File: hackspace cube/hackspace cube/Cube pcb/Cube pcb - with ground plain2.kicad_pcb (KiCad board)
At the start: 2 copper layers, 100 x 64.5 mm, 61 parts, among them J1 Conn_01x09 ( conector 1), J2 Conn_01x09 ( conector 2), J3 Conn_01x02 ( exstra ground co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, J4 Conn_01x14 ( Spare Ports ), Q1 BSS138, Q10 BSS138, Q11 BSS138, Q12 BSS138, Q13 BSS138, Q14 BSS138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

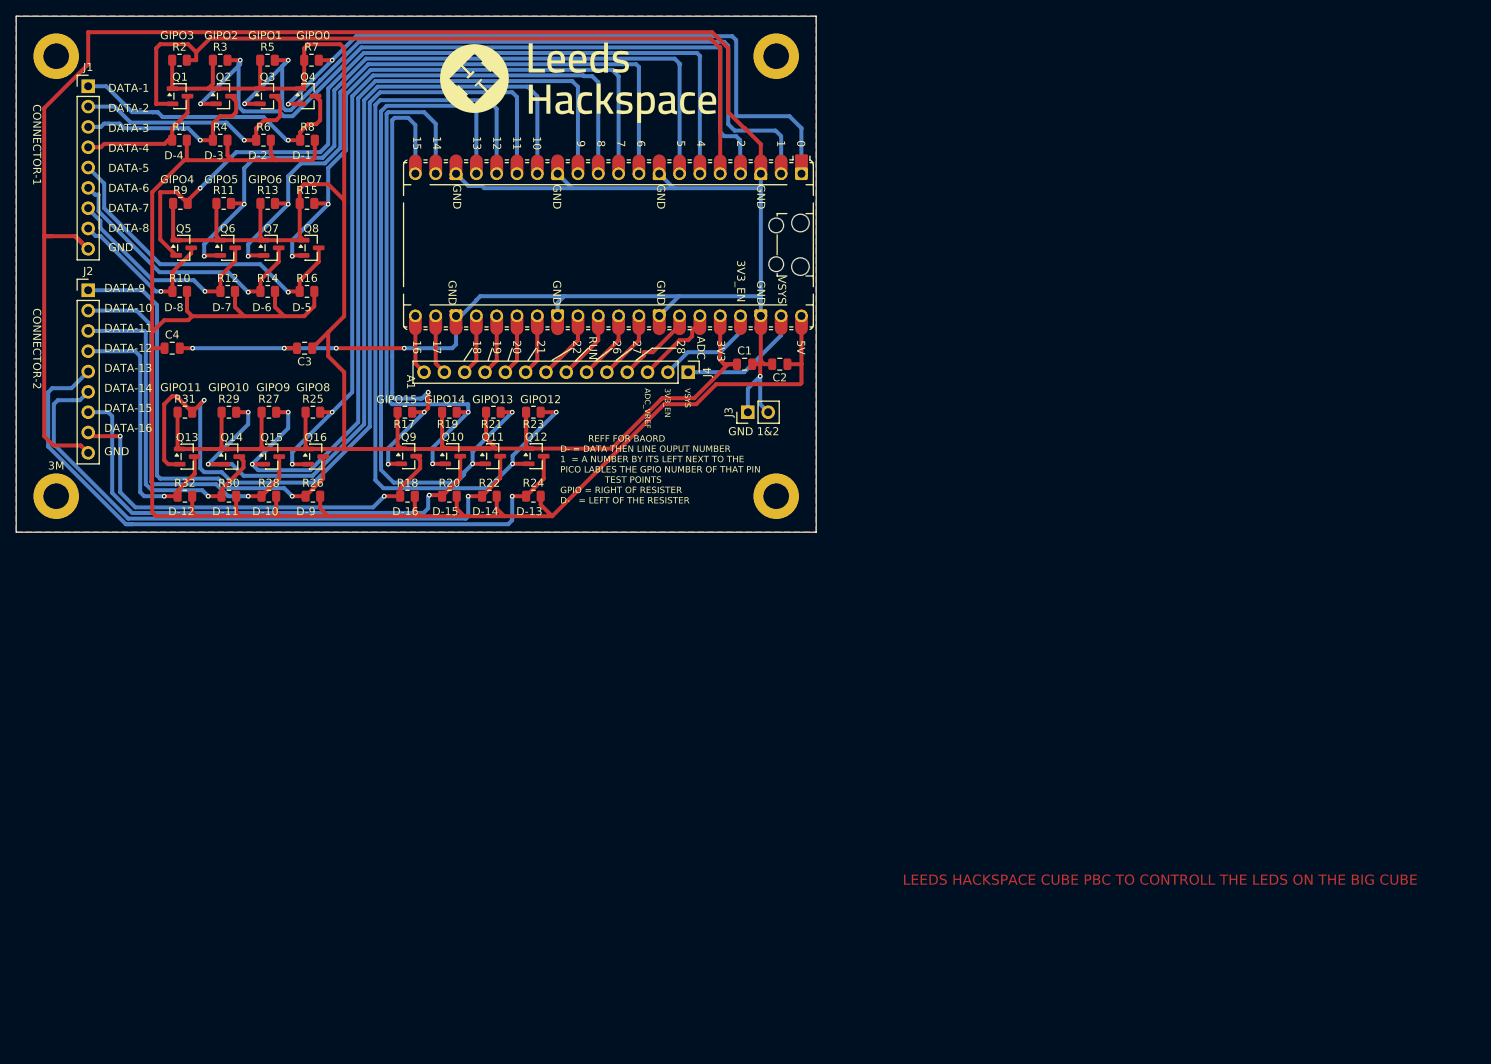
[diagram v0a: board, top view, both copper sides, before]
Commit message: rev 1.4
added new smooth caps and updated pcb
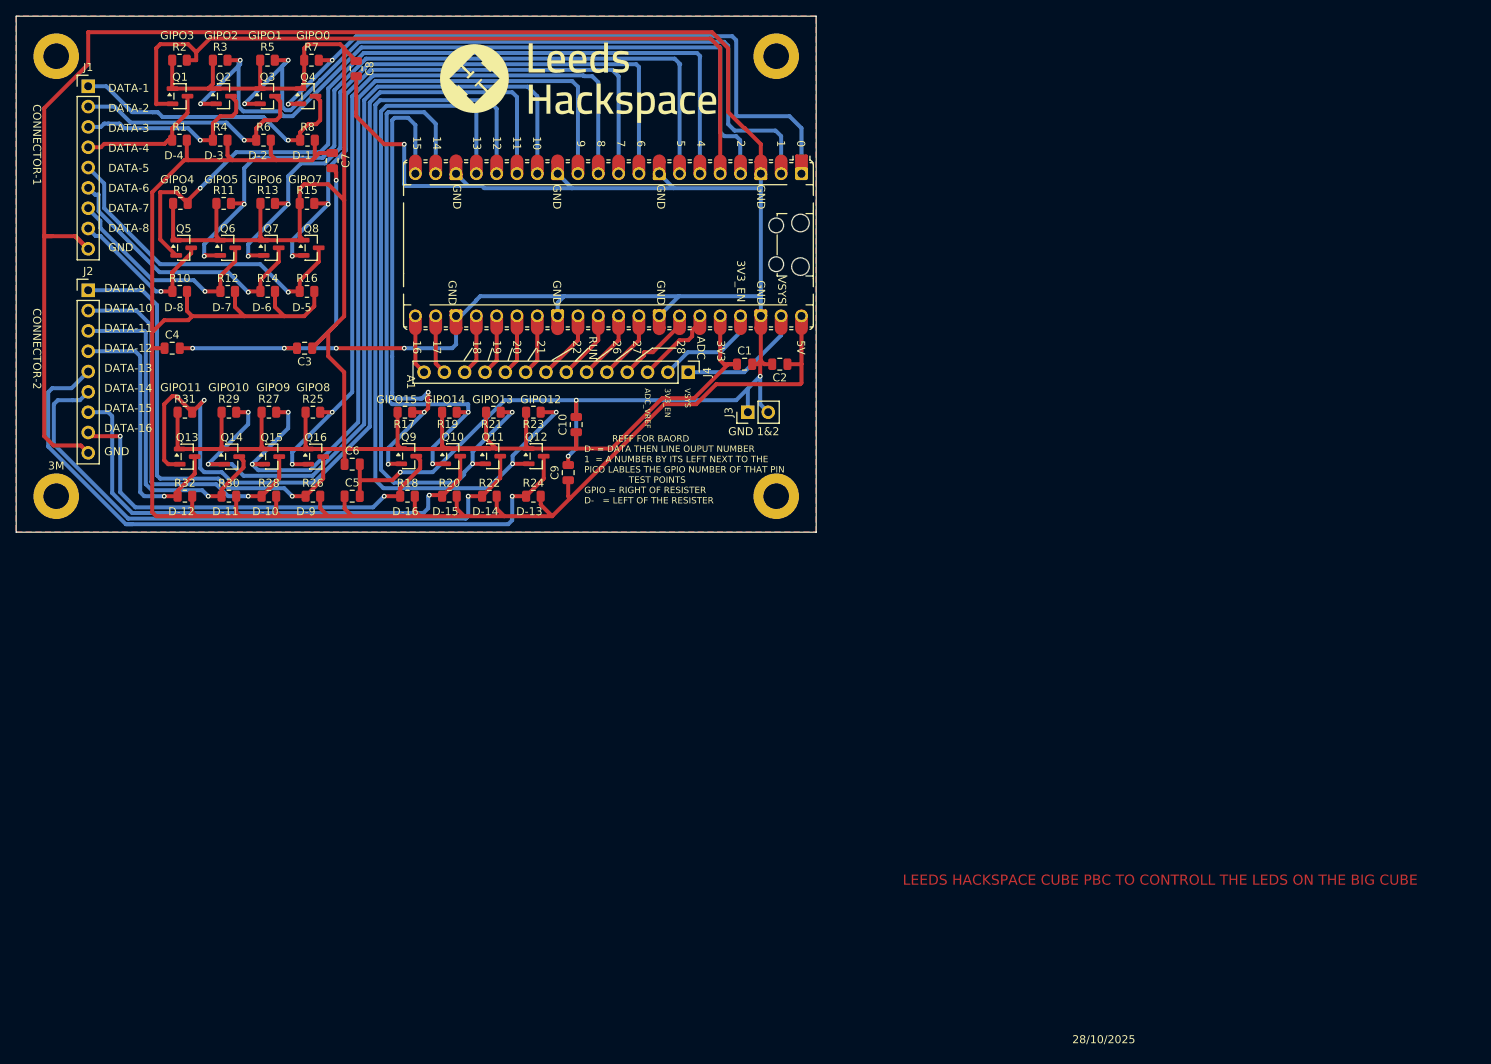
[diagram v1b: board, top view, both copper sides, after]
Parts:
- added C10: 100nF, Capacitor_SMD:C_0805_2012Metric, F.Cu at (145.0, 116.0)
- added C5: 100nF, Capacitor_SMD:C_0805_2012Metric, F.Cu at (117.0, 125.0)
- added C6: 100nF, Capacitor_SMD:C_0805_2012Metric, F.Cu at (117.0, 121.0)
- added C7: 100nF, Capacitor_SMD:C_0805_2012Metric, F.Cu at (114.5, 83.0)
- added C8: 100nF, Capacitor_SMD:C_0805_2012Metric, F.Cu at (117.5, 71.5)
- added C9: 100nF, Capacitor_SMD:C_0805_2012Metric, F.Cu at (144.0, 122.0)
- C1, C2, C3, C4: value C -> 100nF
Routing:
- net GND: track 332.2 -> 449.5 mm, vias 5 -> 10
- net +5V: track 228.2 -> 235.8 mm
- net +3.3V: track 287.8 -> 294.0 mm
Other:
- board text added: "1.4"
- board text added: "28/10/2025"
- board text removed: "1.3"

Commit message: DRC check  done
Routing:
- net GND: track 449.5 -> 448.2 mm
- net DATA-13: track 86.5 -> 85.7 mm
- net DATA-6: track 35.1 -> 35.8 mm
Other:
- board text removed: "1.4"
- board text removed: "CUBE CONTROLL BAORD pcb"
- board text removed: "one"
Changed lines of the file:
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@@
 			(plot_on_all_layers_selection 0x00000000_00000000_00000000_00000000)
 			(disableapertmacros no)
-			(usegerberextensions no)
+			(usegerberextensions yes)
 			(usegerberattributes yes)
 			(usegerberadvancedattributes yes)
@@
 			(sketchdnponfab yes)
 			(crossoutdnponfab yes)
-			(subtractmaskfromsilk no)
+			(subtractmaskfromsilk yes)
 			(outputformat 1)
 			(mirror no)
-			(drillshape 1)
+			(drillshape 0)
 			(scaleselection 1)
-			(outputdirectory "")
+			(outputdirectory "../pcb fab files/")
 		)
 	)
@@
 		(tags "module usb pcb antenna")
 		(property "Reference" "A1"
-			(at 16.2475 24.7025 270)
+			(at 0 0.03 270)
 			(unlocked yes)
 			(layer "F.SilkS")
@@
 	(gr_line
 		(start 146.5 106.5)
-		(end 144.920406 108.079594)
+		(end 145.111874 107.888126)
 		(stroke
 			(width 0.1)
@@
 	(gr_line
 		(start 149.5 106.5)
-		(end 147.5 108)
+		(end 148.055937 107.944063)
 		(stroke
 			(width 0.1)
@@
 		(effects
 			(font
-				(size 0.7 0.7)
+				(size 0.8 0.8)
 				(thickness 0.1)
 			)
@@
 		(effects
 			(font
-				(size 0.7 0.7)
+				(size 0.8 0.8)
 				(thickness 0.1)
 			)
@@
 		(effects
 			(font
-				(size 0.7 0.7)
+				(size 0.8 0.8)
 				(thickness 0.1)
 			)
@@
 		)
 	)
-	(gr_text "CUBE CONTROLL BAORD pcb"
-		(at 187 190 0)
-		(layer "Edge.Cuts")
-		(effects
-			(font
-				(size 1 1)
-				(thickness 0.15)
-			)
-			(justify left bottom)
-		)
-	)
-	(gr_text "one"
-		(at 186.5 183.5 0)
-		(layer "Edge.Cuts")
-		(effects
-			(font
-				(size 1 1)
-				(thickness 0.15)
-			)
-			(justify left bottom)
-		)
-	)
-	(gr_text "1.4\n"
-		(at 269 193.5 0)
-		(layer "Edge.Cuts")
-		(effects
-			(font
-				(size 1 1)
-				(thickness 0.15)
-			)
-			(justify left bottom)
-		)
-	)
 	(segment
 		(start 109.6 94.9)
@@
 	)
 	(segment
-		(start 83.08 118.66)
-		(end 84 119.58)
-		(width 0.5)
-		(layer "F.Cu")
-		(net 6)
-	)
-	(segment
 		(start 84 67)
 		(end 84 71)
@@
 	)
 	(segment
-		(start 86 85.92)
-		(end 84 83.92)
+		(start 93 96)
+		(end 105.5 96)
 		(width 0.5)
 		(layer "B.Cu")
@@
 	)
 	(segment
-		(start 86 89)
-		(end 86 85.92)
+		(start 88.5 88.42)
+		(end 88.5 91.5)
 		(width 0.5)
 		(layer "B.Cu")
@@
 	)
 	(segment
-		(start 93 96)
-		(end 86 89)
+		(start 105.5 96)
+		(end 109 99.5)
 		(width 0.5)
 		(layer "B.Cu")
@@
 	)
 	(segment
-		(start 105.5 96)
-		(end 93 96)
+		(start 84 83.92)
+		(end 88.5 88.42)
 		(width 0.5)
 		(layer "B.Cu")
@@
 	)
 	(segment
-		(start 109 99.5)
-		(end 105.5 96)
+		(start 88.5 91.5)
+		(end 93 96)
 		(width 0.5)
 		(layer "B.Cu")
@@
 	)
 	(segment
-		(start 85.299 87.299)
-		(end 84.839 87.299)
+		(start 87.5 91.5)
+		(end 87.5 88.5)
 		(width 0.5)
 		(layer "B.Cu")
@@
 	)
 	(segment
-		(start 84.839 87.299)
-		(end 84 86.46)
+		(start 87.5 88.5)
+		(end 86.04 88.5)
 		(width 0.5)
 		(layer "B.Cu")
@@
 	)
 	(segment
-		(start 85.299 89.387636)
-		(end 92.911364 97)
+		(start 87.455682 91.544318)
+		(end 87.5 91.5)
 		(width 0.5)
 		(layer "B.Cu")
@@
 	)
 	(segment
-		(start 85.299 87.299)
-		(end 85.299 89.387636)
+		(start 87.455682 91.544318)
+		(end 92.911364 97)
 		(width 0.5)
 		(layer "B.Cu")
@@
 	)
 	(segment
+		(start 86.04 88.5)
+		(end 84 86.46)
+		(width 0.5)
+		(layer "B.Cu")
+		(net 37)
+	)
+	(segment
 		(start 99.5875 80.5)
 		(end 98 80.5)
@@
 		(width 0.5)
 		(layer "B.Cu")
-		(net 43)
-	)
-	(segment
-		(start 88.709636 128.5)
-		(end 89.5 128.5)
-		(width 0.5)
-		(layer "B.Cu")
